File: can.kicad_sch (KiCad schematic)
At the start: 7 parts, among them J401 Conn_01x04, U401 SN65HVD232

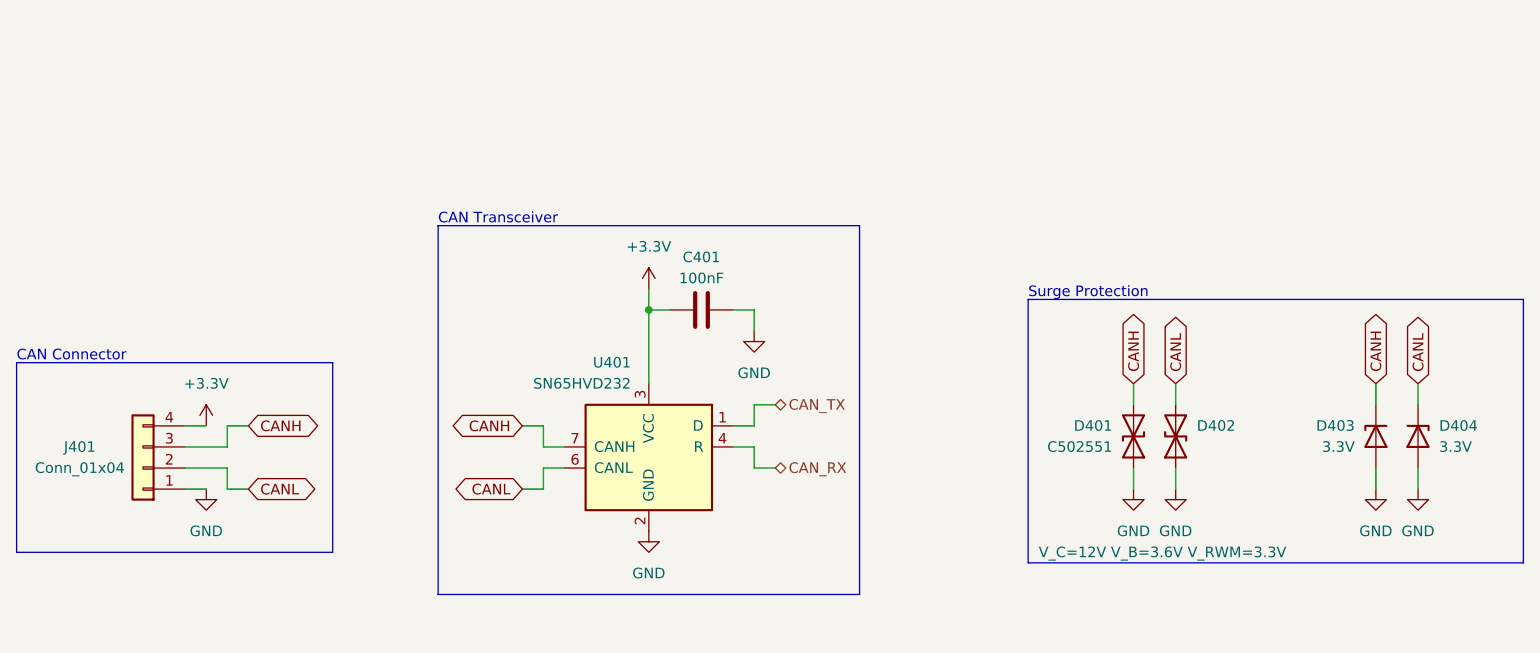
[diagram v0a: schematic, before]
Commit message: Reworked DisplayBoard circuitry and layout; v1.1
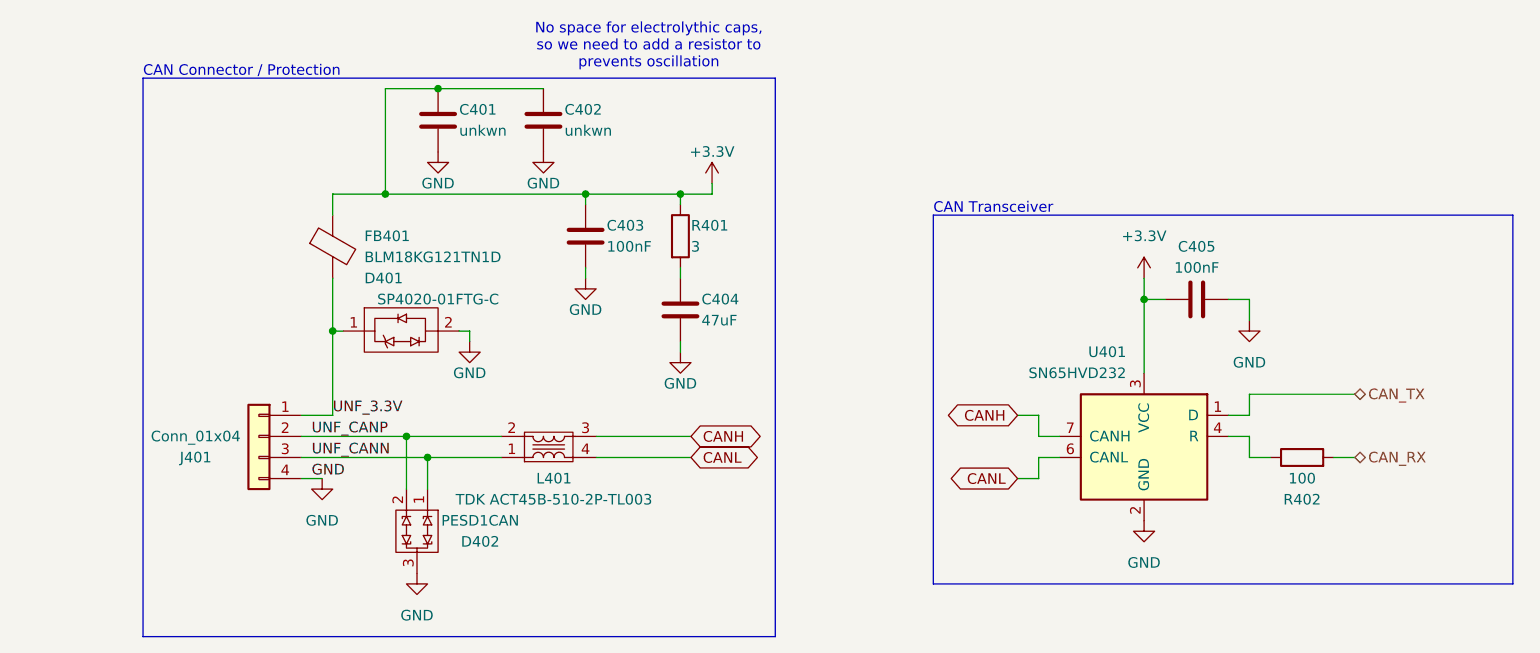
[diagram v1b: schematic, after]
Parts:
- removed D401: C502551, Diode_SMD:D_SOD-882, symbol Device:D_TVS
- removed D402: V_C=12V V_B=3.6V V_RWM=3.3V, Diode_SMD:D_SOD-882, symbol Device:D_TVS
- removed D403, D404: 3.3V, Diode_SMD:D_SOD-123, symbol Device:D_Zener
- added C401, C402: unkwn, Capacitor_SMD:C_0805_2012Metric, symbol Device:C
- added C403: 100nF, Capacitor_SMD:C_0805_2012Metric, symbol Device:C
- added C404: 47uF, Capacitor_SMD:C_0805_2012Metric, symbol Device:C
- added D401: SP4020-01FTG-C, Resistor_SMD:R_0805_2012Metric, symbol CustomSymbols:SP4020-01FTG-C
- added D402: PESD1CAN, Package_TO_SOT_SMD:SOT-23, symbol CustomSymbols:PESD1CAN
- added FB401: BLM18KG121TN1D, Inductor_SMD:L_0603_1608Metric, symbol Device:FerriteBead
- added L401: TDK ACT45B-510-2P-TL003, CustomFootprints:TDK ACT45B-510-2P-TL003, symbol CustomSymbols:TDK_ACT45B-510-2P-TL003
- added R401: 3, Resistor_SMD:R_0603_1608Metric, symbol Device:R
- added R402: 100, Resistor_SMD:R_0603_1608Metric, symbol Device:R
- J401: footprint Connector_JST:JST_XH_B4B-XH-A_1x04_P2.50mm_Vertical -> CustomFootprints:JST_PH_B4B_SM4_TB
- renumbered C401 to C405
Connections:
- net +3.3V: now also C401.1, C402.1, C403.1, FB401.1, R401.1; no longer J401.4 (Pin_4)
- net CANH: now also L401.3; no longer J401.3 (Pin_3)
- net CANL: now also L401.4; no longer J401.2 (Pin_2)
- net CAN_RX: now also R402.2; no longer U401.4 (R)
- net GND: now also J401.4 (Pin_4), C401.2, C402.2, C403.2, C404.2, D401.2, D402.3; no longer J401.1 (Pin_1)
- new net: C404.1, R401.2
- new net: R402.1, U401.4 (R)
- new net UNF_3.3V: D401.1, FB401.2, J401.1 (Pin_1)
- new net UNF_CANN: D402.1, J401.3 (Pin_3), L401.1
- new net UNF_CANP: D402.2, J401.2 (Pin_2), L401.2
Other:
- note added: "CAN Connector / Protection"
- note added: "No space for electrolythic caps, so we need to add a resistor to prevents oscillation"
- note removed: "CAN Connector"
- note removed: "Surge Protection"
- moved on the sheet: C405, J401, U401

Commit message: Finished v1.1
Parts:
- removed D401: SP4020-01FTG-C, Resistor_SMD:R_0805_2012Metric, symbol CustomSymbols:SP4020-01FTG-C
- added C12: 47uF, Capacitor_SMD:C_0805_2012Metric, symbol Device:C
- added D1: SP4020-01FTG-C, Resistor_SMD:R_0805_2012Metric, symbol CustomSymbols:SP4020-01FTG-C
- added R11: 3, Resistor_SMD:R_0603_1608Metric, symbol Device:R
- J3: renamed from J401; footprint CustomFootprints:JST_PH_B4B_SM4_TB -> Connector_JST:JST_PH_B4B-PH-SM4-TB_1x04-1MP_P2.00mm_Vertical
- renumbered C403 to C10, C404 to C11, C405 to C13, C401 to C8, C402 to C9, D402 to D2, FB401 to FB1, L401 to L2, R401 to R10, R402 to R12, U401 to U2
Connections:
- net +3.3V: now also R11.1
- net GND: now also J3.1 (Pin_1), C12.2, D1.2; no longer J3.4 (Pin_4)
- net UNF_3.3V: now also J3.4 (Pin_4), D1.1; no longer J3.1 (Pin_1)
- net UNF_CANN: now also D2.2, J3.2 (Pin_2), L2.2; no longer D2.1, J3.3 (Pin_3), L2.1
- net UNF_CANP: now also D2.1, J3.3 (Pin_3), L2.1; no longer D2.2, J3.2 (Pin_2), L2.2
- net CANH renamed CAN+
- net CAN+: now also L2.4; no longer L2.3
- net CANL renamed CAN-
- net CAN-: now also L2.3; no longer L2.4
- new net: C12.1, R11.2
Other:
- note added: "No space for electrolythic cap, so a resistor is needed to prevent oscillation"
- note removed: "No space for electrolythic caps, so we need to add a resistor to prevents oscillation"
- moved on the sheet: D2, J3

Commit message: Silkscreen touchups & gerbers
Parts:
- D1: footprint Resistor_SMD:R_0805_2012Metric -> Diode_SMD:D_SOD-323
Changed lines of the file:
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@@
 			)
 		)
-		(property "Footprint" "Resistor_SMD:R_0805_2012Metric"
+		(property "Footprint" "Diode_SMD:D_SOD-323"
 			(at 101.346 75.438 0)
 			(hide yes)
